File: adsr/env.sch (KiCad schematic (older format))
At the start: 29 parts, among them J10 Conn_01x08_Male, J9 Conn_01x08_Female, Q1 2N3904, Q2 2N3904, Q5 DMMT5401, U1 LM13700, U2 TL074, U3 DG403, U4 DG403

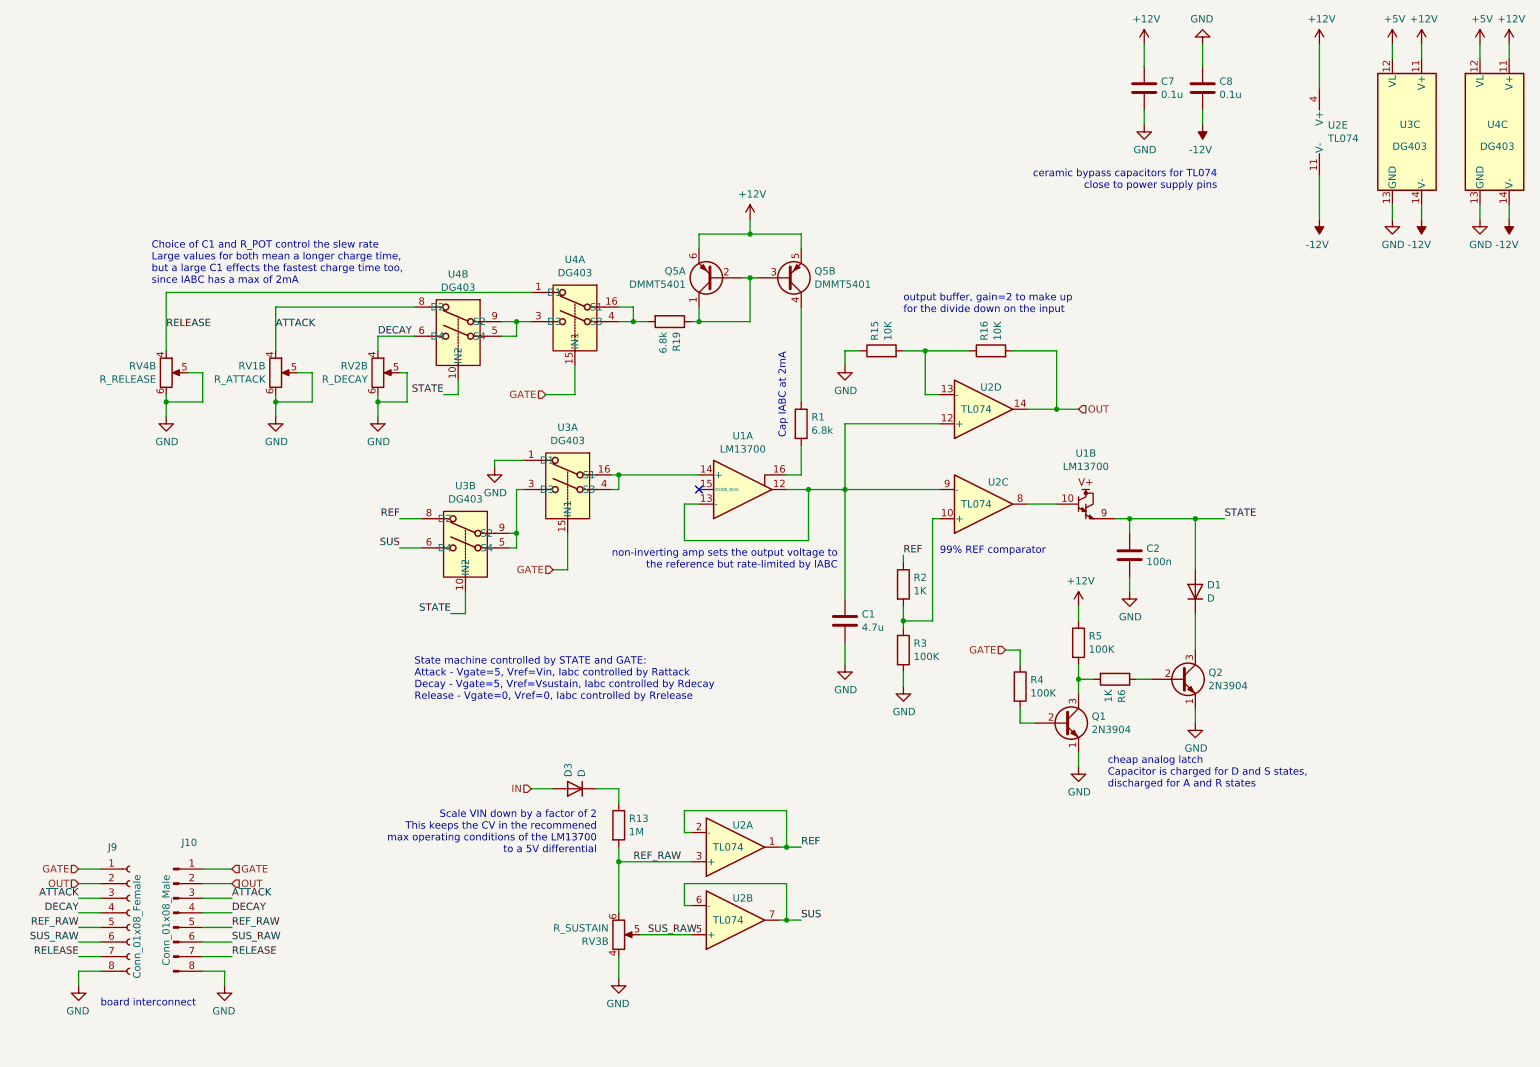
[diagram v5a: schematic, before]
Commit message: reduce to one input
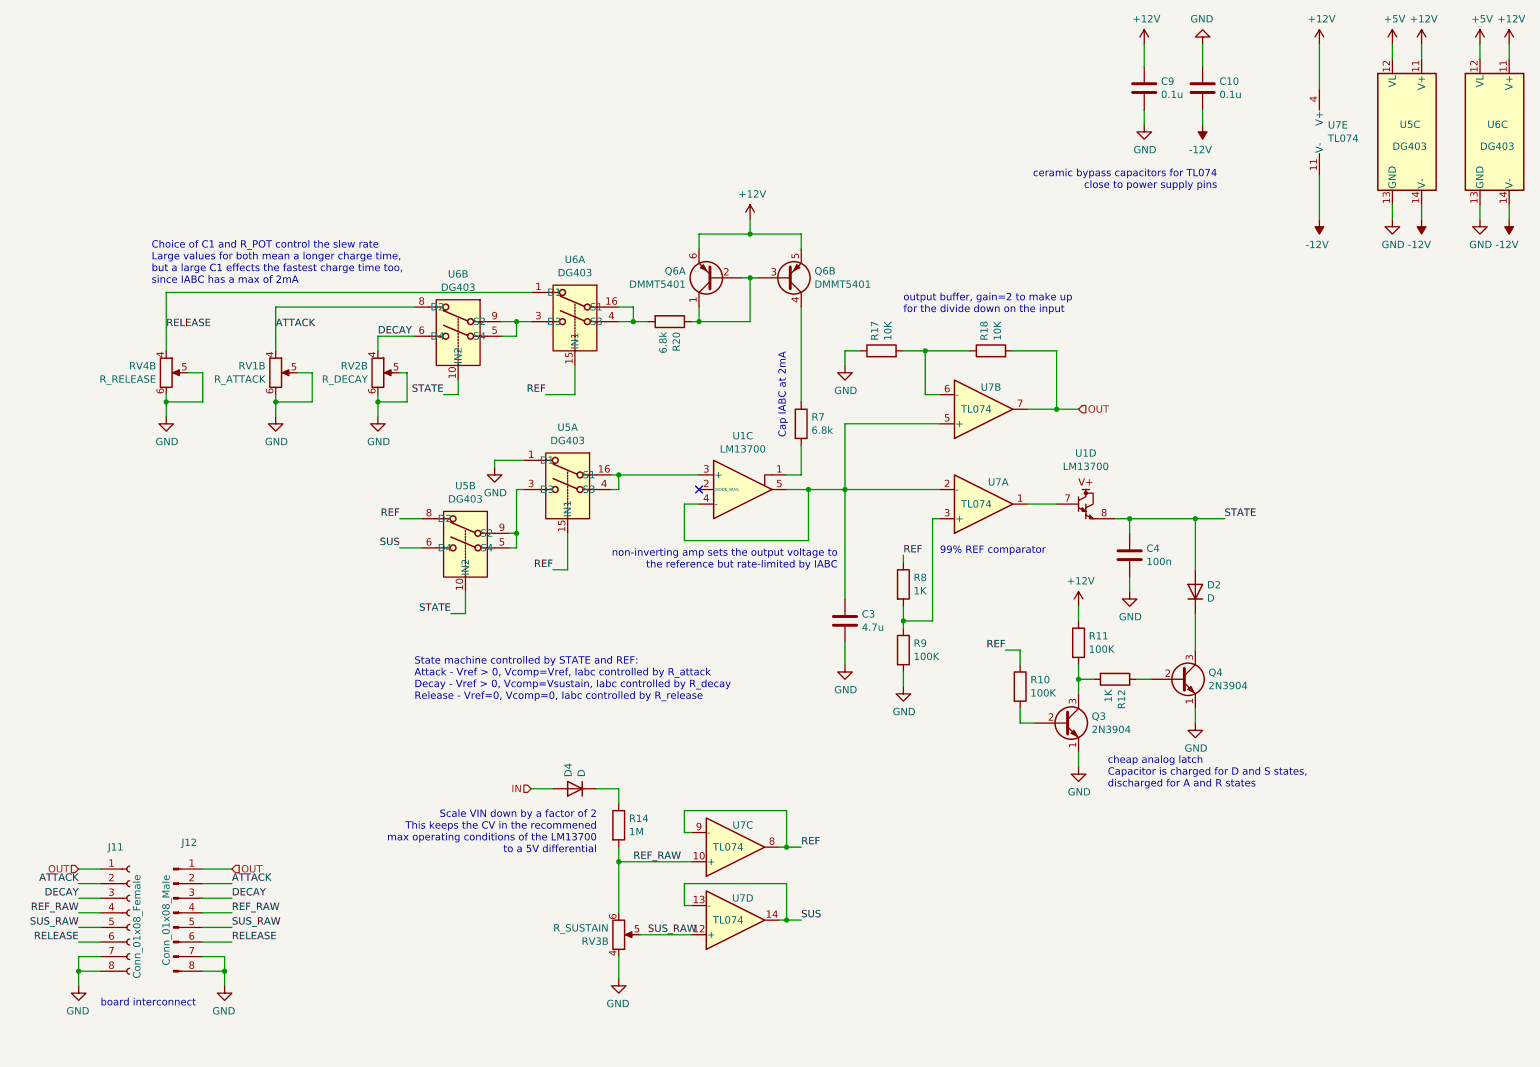
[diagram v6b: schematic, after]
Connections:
- net ATTACK: now also J10.2 (Pin_2), J9.2 (Pin_2); no longer J10.3 (Pin_3), J9.3 (Pin_3)
- net DECAY: now also J10.3 (Pin_3), J9.3 (Pin_3); no longer J10.4 (Pin_4), J9.4 (Pin_4)
- net GND: now also J10.7 (Pin_7), J9.7 (Pin_7)
- net OUT: now also J10.1 (Pin_1), J9.1 (Pin_1), U2.7; no longer J10.2 (Pin_2), J9.2 (Pin_2), U2.14
- net REF: now also R4.1, U2.8, U2.9 (-), U3.15 (IN1), U4.15 (IN1); no longer U2.1, U2.2 (-)
- net REF_RAW: now also J10.4 (Pin_4), J9.4 (Pin_4), U2.10 (+); no longer J10.5 (Pin_5), J9.5 (Pin_5), U2.3 (+)
- net RELEASE: now also J10.6 (Pin_6), J9.6 (Pin_6); no longer J10.7 (Pin_7), J9.7 (Pin_7)
- net STATE: now also U1.8; no longer U1.9
- net SUS: now also U2.13 (-), U2.14; no longer U2.6 (-), U2.7
- net SUS_RAW: now also J10.5 (Pin_5), J9.5 (Pin_5), U2.12 (+); no longer J10.6 (Pin_6), J9.6 (Pin_6), U2.5 (+)
- net at R15.2, R16.1: now also U2.6 (-); no longer U2.13 (-)
- net at U3.16 (S1), U3.4 (S3): now also U1.3 (+); no longer U1.14 (+)
- net at R1.2: now also U1.1; no longer U1.16
- net at R2.2, R3.1: now also U2.3 (+); no longer U2.10 (+)
- removed net GATE: J10.1 (Pin_1), J9.1 (Pin_1), R4.1, U3.15 (IN1), U4.15 (IN1)
- new net: C1.1, U1.4 (-), U1.5, U2.2 (-), U2.5 (+)
- new net: U1.7, U2.1
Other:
- note added: "State machine controlled by STATE and REF:\nAttack - Vref > 0, Vcomp=Vref, Iabc controlled by R_attack\nDecay - Vref > 0, Vcomp=Vsustain, Iabc controlled by R_decay\nRelease - Vref=0, Vcomp=0, Iabc controlled by R_release\n"
- note removed: "State machine controlled by STATE and GATE:\nAttack - Vgate=5, Vref=Vin, Iabc controlled by Rattack\nDecay - Vgate=5, Vref=Vsustain, Iabc controlled by Rdecay\nRelease - Vgate=0, Vref=0, Iabc controlled by Rrelease\n"

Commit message: adsr improvements
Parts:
- removed C1: 4.7u, Capacitor_SMD:C_1206_3216Metric_Pad1.42x1.75mm_HandSolder, symbol Device:C
- added C11: 4.7u, Capacitor_SMD:C_1206_3216Metric_Pad1.42x1.75mm_HandSolder, symbol Device:C
- added R21: 1K, Resistor_SMD:R_1206_3216Metric_Pad1.42x1.75mm_HandSolder, symbol Device:R
- added R22: 100K, Resistor_SMD:R_1206_3216Metric_Pad1.42x1.75mm_HandSolder, symbol Device:R
- added U8: TL072, Package_DIP:DIP-8_W7.62mm, symbol Amplifier_Operational:TL072
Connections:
- net +12V: now also R22.2
- net ATTACK: now also J10.3 (Pin_3), J9.3 (Pin_3), RV1.1; no longer J10.2 (Pin_2), J9.2 (Pin_2), RV1.4
- net DECAY: now also J10.4 (Pin_4), J9.4 (Pin_4), RV2.1; no longer J10.3 (Pin_3), J9.3 (Pin_3), RV2.4
- net GND: now also RV1.2, RV1.3, RV2.2, RV2.3, RV3.1, RV4.2, RV4.3, C11.2, R21.2; no longer J10.7 (Pin_7), J9.7 (Pin_7), RV1.5, RV1.6, RV2.5, RV2.6, RV3.4, RV4.5, RV4.6
- net OUT: now also J10.2 (Pin_2), J9.2 (Pin_2), U2.8; no longer J10.1 (Pin_1), J9.1 (Pin_1), U2.7
- net REF: now also U2.1, U2.2 (-); no longer R4.1, U2.8, U2.9 (-), U3.15 (IN1), U4.15 (IN1)
- net REF_RAW: now also J10.5 (Pin_5), J9.5 (Pin_5), RV3.3, U2.3 (+); no longer J10.4 (Pin_4), J9.4 (Pin_4), RV3.6, U2.10 (+)
- net RELEASE: now also J10.7 (Pin_7), J9.7 (Pin_7), RV4.1; no longer J10.6 (Pin_6), J9.6 (Pin_6), RV4.4
- net STATE: now also U1.9; no longer U1.8
- net SUS: now also U2.6 (-), U2.7; no longer U2.13 (-), U2.14
- net SUS_RAW: now also J10.6 (Pin_6), J9.6 (Pin_6), RV3.2, U2.5 (+); no longer J10.5 (Pin_5), J9.5 (Pin_5), RV3.5, U2.12 (+)
- net IN_RAW: now reaches D3.1 (K), R13.1
- net IN_RAW: now also J10.1 (Pin_1), J9.1 (Pin_1), U2.12 (+)
- net at R15.2, R16.1: now also U2.9 (-); no longer U2.6 (-)
- net at R1.2: now also U1.16; no longer U1.1
- net at U3.16 (S1), U3.4 (S3): now also U1.14 (+); no longer U1.3 (+)
- net at R2.2, R3.1: now also U8.2 (-); no longer U2.3 (+)
- new net: R21.1, R22.1, U2.13 (-)
- new net: U1.10, U8.1
- new net VC: C11.1, U1.12, U1.13 (-), U2.10 (+), U8.3 (+)
- new net VINS: R4.1, U2.14, U3.15 (IN1), U4.15 (IN1)
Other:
- note added: "Choice of C1 and R_POT control the slew rate\nLarge values for both mean a longer charge time,\nbut a large C1 effects the fastest charge time too,\nsince IABC has a max of 2mA\n\nAudio taper gives finer control at lower rates"
- note added: "This comparator for VIN > 119mV\nallows operating at very low VIN"
- note removed: "Choice of C1 and R_POT control the slew rate\nLarge values for both mean a longer charge time,\nbut a large C1 effects the fastest charge time too,\nsince IABC has a max of 2mA"
- moved on the sheet: D3, R13
